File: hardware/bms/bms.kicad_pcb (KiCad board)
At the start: 2 copper layers, 199 parts, among them J1 Conn_01x08, J10 Conn_01x02, J11 Conn_01x02, J12 Conn_01x02, J13 Conn_01x10, J14 Conn_01x02, J15 Conn_01x02, J16 Cell Bypass, J2 Conn_01x04, J3 USB_B_Micro, J4 Conn_01x05, J5 Conn_01x04, J6 Conn_01x04, J7 Conn_01x03, J8 Conn_01x03, J9 Conn_01x02, M1 MountingHole, M2 MountingHole, M3 MountingHole, M4 MountingHole, M5 MountingHole, M6 MountingHole, Q1 BC817, Q10 ZXMP4A16G, Q11 IRF540N, Q12 IRF540N, Q13 BSS138, Q14 IRF540N, Q15 BSS138, Q16 BSS138, Q2 ZXMP4A16G, Q3 BSS138, Q4 BS170, Q5 IRF9540N, Q6 BC847, Q7 IRF9540N, Q8 BSS138, Q9 ZXMP4A16G, SW1 SW_DIP_x03, U1 USBLC6-2SC6, U2 STM32F042C6Tx, U3 TPS560430x3F, U4 TCAN334, U5 MAX485E, U6 LM5164DDAR, U7 LSI94202, Y1 8MHz

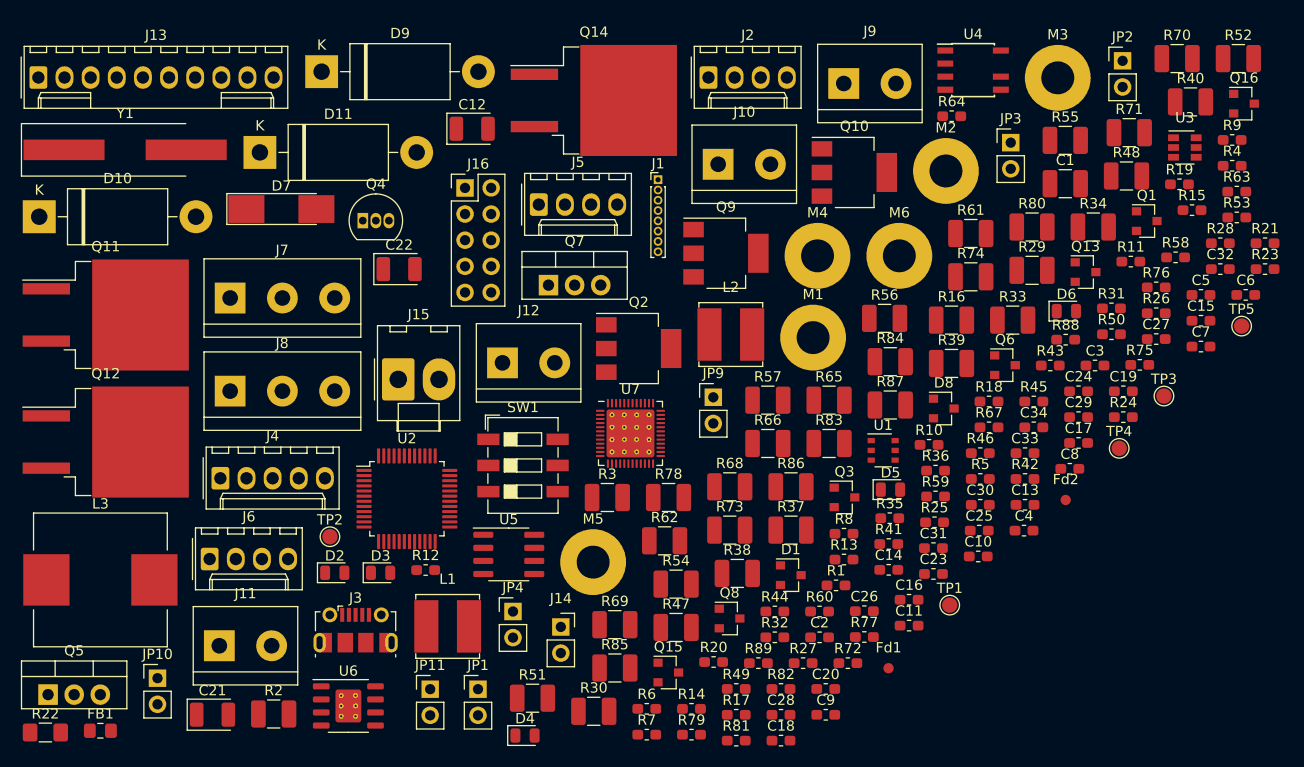
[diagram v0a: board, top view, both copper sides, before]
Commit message: footprint corrections
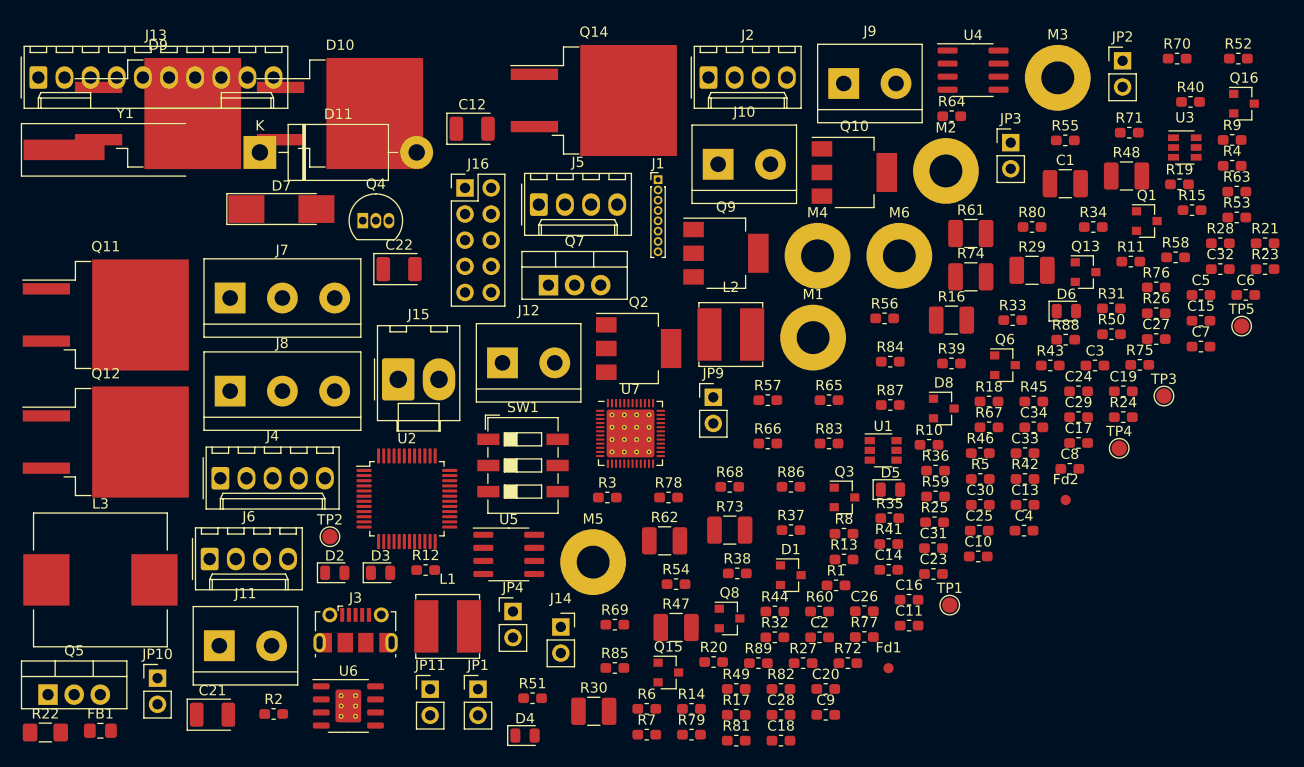
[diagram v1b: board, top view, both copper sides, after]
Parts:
- D10, D9: value MBR340 -> 200V_Diode; footprint Diode_THT:D_DO-201AD_P15.24mm_Horizontal -> bms:D2PAK
- R2, R3, R33, R34, R37, R38, R39, R40, R51, R52, R54, R55, R56, R57, R65, R66, R68, R69, R70, R71, R78, R80, R83, R84, R85, R86, R87: footprint Resistor_SMD:R_1210_3225Metric_Pad1.42x2.65mm_HandSolder -> Resistor_SMD:R_0603_1608Metric_Pad1.05x0.95mm_HandSolder
- R35: value 1K -> 10K
- U1: footprint Package_SO:TSOP-6_1.65x3.05mm_P0.95mm -> Package_TO_SOT_SMD:SuperSOT-6
- U4: footprint Package_SO:SOIC-8-N7_3.9x4.9mm_P1.27mm -> Package_SO:SOIC-8_3.9x4.9mm_P1.27mm
- moved D10 30.9 mm to (177.2, 75.5)
- moved D9 16.4 mm to (159.5, 75.5)
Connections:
- C23 pad 1: PWR- -> Net-(C23-Pad1)
- D10 pad 1: Net-(D10-Pad1) -> PWR-
- D9 pad 1: Net-(C16-Pad2) -> Net-(D9-Pad1)
- L3 pad 1: Net-(D10-Pad1) -> Net-(D10-Pad4)
- Q1 pad 2: Net-(D9-Pad2) -> Net-(D9-Pad1)
- Q14 pad 2: LOAD -> CS2
- Q14 pad 3: CS1 -> LOAD
- Q5 pad 1: Net-(D9-Pad2) -> Net-(D9-Pad1)
- Q5 pad 2: Net-(D10-Pad1) -> Net-(D10-Pad4)
- Q7 pad 1: PWR- -> Net-(C23-Pad1)
- R35 pad 2: Net-(D9-Pad2) -> Net-(D9-Pad1)
- R36 pad 1: Net-(D9-Pad2) -> Net-(D9-Pad1)
- R46 pad 1: PWR- -> Net-(C23-Pad1)
- R89 pad 2: LOAD -> CHG

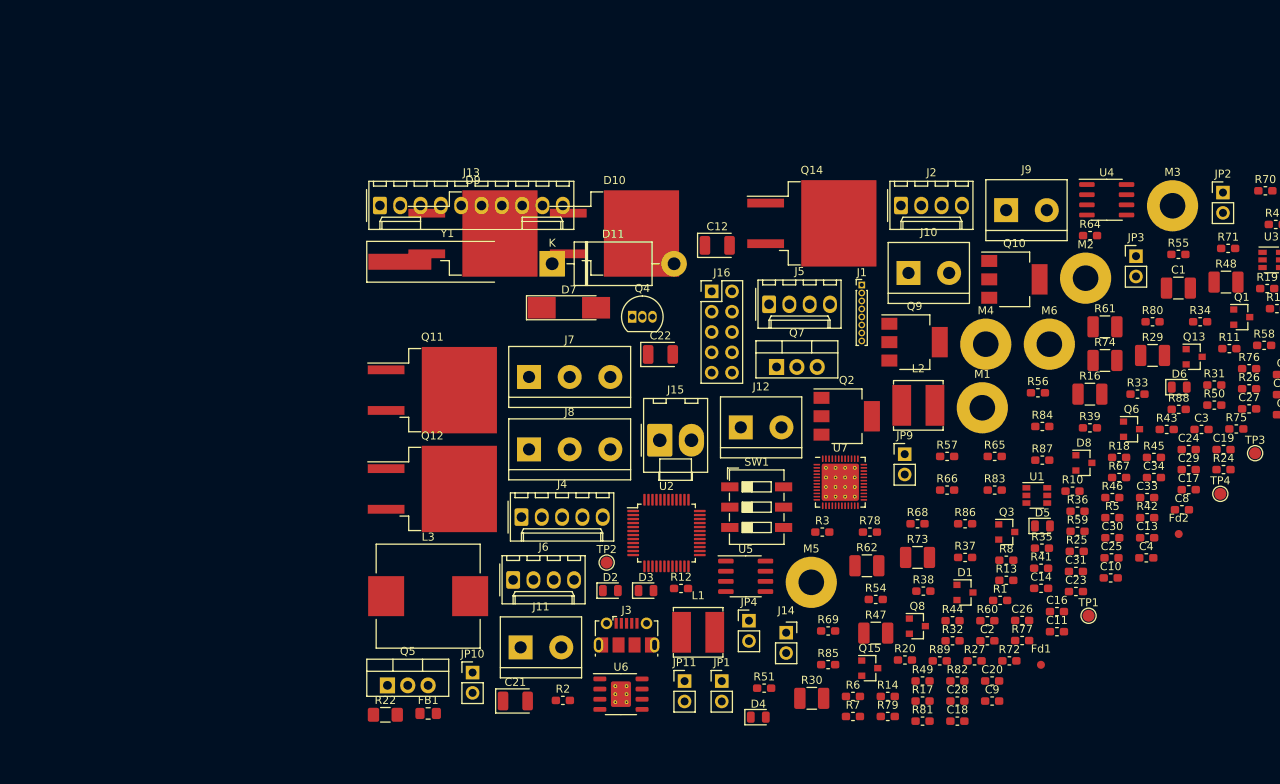
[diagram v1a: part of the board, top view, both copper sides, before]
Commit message: Added i2c level shifter
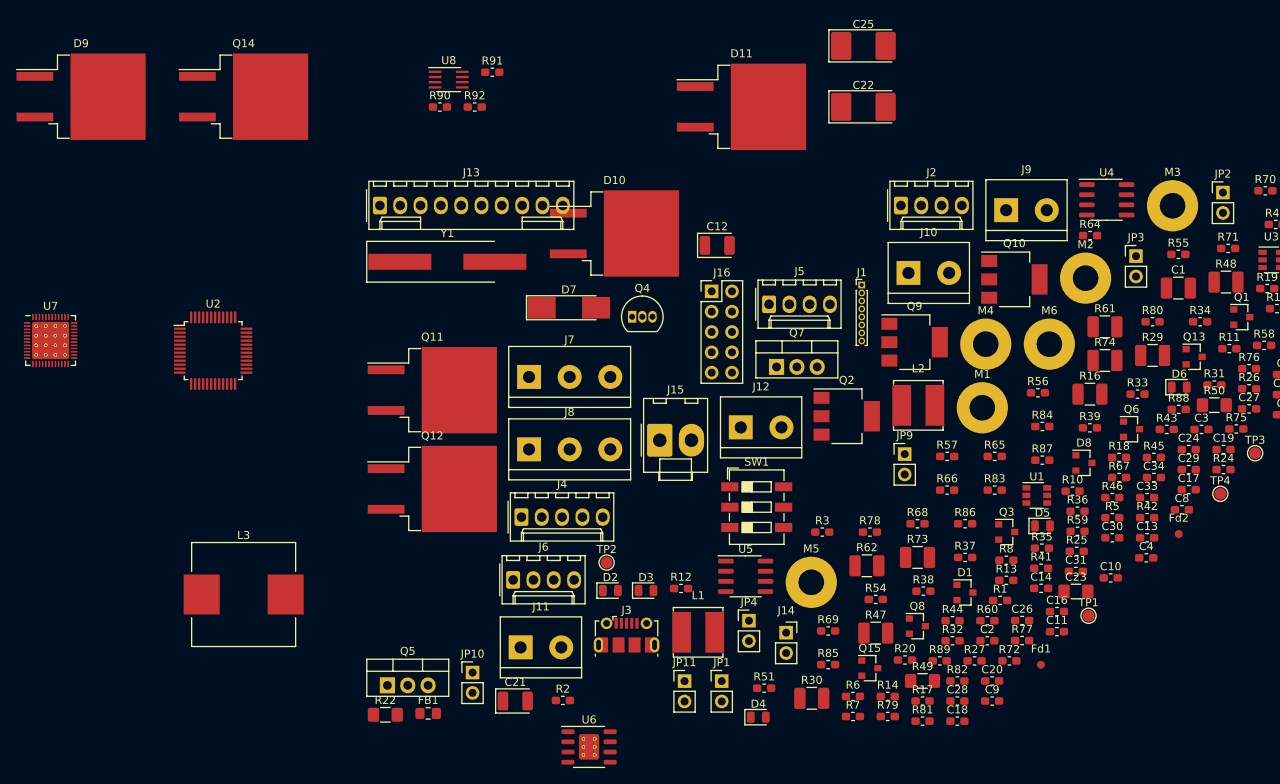
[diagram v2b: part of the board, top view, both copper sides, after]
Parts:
- added R90: 4K7, Resistor_SMD:R_0603_1608Metric_Pad1.05x0.95mm_HandSolder, F.Cu at (155.3, 59.7)
- added R91: 4K7, Resistor_SMD:R_0603_1608Metric_Pad1.05x0.95mm_HandSolder, F.Cu at (161.9, 55.4)
- added R92: 200K, Resistor_SMD:R_0603_1608Metric_Pad1.05x0.95mm_HandSolder, F.Cu at (159.7, 59.7)
- added U8: PCA9306, Package_SO:SSOP-8_2.95x2.8mm_P0.65mm, F.Cu at (156.4, 56.3)
- C22: value 330uF -> 10uF; footprint Capacitor_Tantalum_SMD:CP_EIA-3528-21_Kemet-B -> Capacitor_Tantalum_SMD:CP_EIA-7132-28_AVX-C
- C23: value 10nF -> 0.01uF; footprint Capacitor_SMD:C_0603_1608Metric_Pad1.05x0.95mm_HandSolder -> Capacitor_SMD:C_1206_3216Metric_Pad1.42x1.75mm_HandSolder
- C25: value 2.2uF -> 10uF; footprint Capacitor_SMD:C_0603_1608Metric_Pad1.05x0.95mm_HandSolder -> Capacitor_Tantalum_SMD:CP_EIA-7132-28_AVX-C
- D11: value MBR340 -> 200V_Diode; footprint Diode_THT:D_DO-201AD_P15.24mm_Horizontal -> bms:D2PAK
- R49, R50: footprint Resistor_SMD:R_0603_1608Metric_Pad1.05x0.95mm_HandSolder -> Resistor_SMD:R_1206_3216Metric_Pad1.42x1.75mm_HandSolder
- R6, R9: value 2K2 -> 4K7
- moved U7 100.3 mm to (106.7, 88.9)
- moved Q14 72.8 mm to (130.8, 58.4)
- moved C25 71.1 mm to (208.3, 52.1)
- moved U2 61.1 mm to (127.0, 90.2)
- moved D9 51.9 mm to (110.5, 58.4)
- moved C22 40.0 mm to (208.3, 59.7)
- moved D11 30.7 mm to (193.0, 59.7)
- moved L3 23.1 mm to (130.8, 120.7)
- moved U6 7.71 mm to (174.0, 139.7)
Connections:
- net Net-(TP5-Pad1) renamed RGO
- C25 pad 1: PWR- -> Net-(C22-Pad1)
- C25 pad 2: Net-(C22-Pad1) -> PWR-
- D11 pad 1: PWR_OUT -> Net-(C22-Pad1)
- R6 pad 1: SDA -> SDA_3.3
- R89 pad 2: CHG -> LOAD
- R9 pad 1: SCL -> SCL_3.3
- U2 pad 42: SCL -> SCL_3.3
- U2 pad 43: SDA -> SDA_3.3
- U7 pad 49: (no net) -> GND

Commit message: Schematics and footprint corrections
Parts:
- added FB2: Ferrite_Bead_Small, Inductor_SMD:L_0805_2012Metric_Pad1.15x1.40mm_HandSolder, F.Cu at (96.5, 156.2)
- added NT1: Net-Tie_2, NetTie:NetTie-2_THT_Pad1.0mm, F.Cu at (248.9, 128.3)
- Q10, Q2, Q9: value ZXMP4A16G -> NX3008PBK; footprint Package_TO_SOT_SMD:SOT-223-3_TabPin2 -> Package_TO_SOT_SMD:SOT-23
- Q4: footprint Package_TO_SOT_THT:TO-92_Inline -> Package_TO_SOT_SMD:SOT-23W_Handsoldering
- Q5, Q7: footprint Package_TO_SOT_THT:TO-220-3_Vertical -> Package_TO_SOT_SMD:TO-263-2
- moved U3 217.9 mm to (54.6, 153.7)
- moved C1 216.7 mm to (44.5, 157.5)
- moved C3 207.7 mm to (49.5, 152.4)
- moved R4 202.2 mm to (82.5, 170.2)
- moved R43 199.4 mm to (47.0, 90.2)
- moved C8 199.2 mm to (54.6, 157.5)
- moved R46 198.0 mm to (41.9, 94.0)
- moved C23 195.3 mm to (41.9, 90.2)
- moved R9 194.9 mm to (84.2, 153.7)
- moved R16 190.3 mm to (58.4, 162.6)
- moved R53 189.7 mm to (77.5, 118.1)
- moved Q6 188.6 mm to (53.3, 91.4)
- moved R41 185.0 mm to (47.0, 94.0)
- moved R23 184.6 mm to (83.8, 68.6)
- moved C15 183.4 mm to (81.3, 58.4)
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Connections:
- C10 pad 2: GND -> GNDS
- C18 pad 2: GND -> GNDA
- C19 pad 2: GND -> GNDA
- C26 pad 2: GND -> GNDA
- C27 pad 2: GND -> GNDA
- C31 pad 2: GND -> GNDA
- C32 pad 2: GND -> GNDA
- C33 pad 2: GND -> GNDA
- C34 pad 2: GND -> GNDA
- JP10 pad 2: GND -> GNDA
- JP3 pad 2: GND -> GNDA
- R50 pad 1: GND -> GNDA
- R76 pad 1: VCC -> RGO
- R77 pad 1: VCC -> RGO
- R79 pad 1: VCC -> RGO
- R82 pad 1: VCC -> RGO
- R88 pad 2: GND -> GNDA
- U2 pad 8: GNDA -> GNDS
- U7 pad 18: GND -> GNDA
- U7 pad 28: GND -> GNDA
- U7 pad 29: GND -> GNDA
- U7 pad 49: GND -> GNDA

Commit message: Started placement
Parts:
- C16, C22, C25, C34, D10, L3, Q4, R29, R30, R33, R34, R37, R39, R47, R48, R51, R52, R54, R56, R61, R62, R65, R66, R68, R70, R73, R74, R78, R83, R87: moved to B.Cu
- moved JP9 121.1 mm to (53.0, 80.7), turned to 90 degrees
- moved Q16 115.5 mm to (193.6, 148.3)
- moved C12 112.7 mm to (105.6, 62.0), turned to 0 degrees
- moved JP3 112.0 mm to (73.4, 80.5), turned to 90 degrees
- moved D10 111.1 mm to (30.3, 45.3)
- moved TP1 109.7 mm to (109.7, 63.0)
- moved R16 107.8 mm to (105.7, 65.7), turned to 180 degrees
- moved D11 107.8 mm to (30.4, 69.5)
- moved JP2 104.9 mm to (65.1, 80.3), turned to 90 degrees
- moved C22 103.4 mm to (27.0, 71.0)
- moved Q13 103.2 mm to (200.0, 141.5)
- moved Q8 102.9 mm to (207.8, 148.4)
- moved C1 102.8 mm to (101.5, 72.0), turned to 270 degrees
- moved D1 102.7 mm to (105.2, 69.5), turned to 270 degrees
- moved Q1 102.3 mm to (17.0, 48.2)
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
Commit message: Changed placement
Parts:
- moved Q12 47.3 mm to (49.0, 87.3), turned to 180 degrees
- moved R64 41.5 mm to (51.5, 60.5), turned to 0 degrees
- moved R59 40.2 mm to (51.5, 58.2), turned to 0 degrees
- moved C28 34.1 mm to (55.6, 58.2), turned to 180 degrees
- moved C14 33.1 mm to (63.1, 45.7)
- moved C15 33.1 mm to (77.4, 42.6)
- moved C20 33.1 mm to (85.0, 42.6)
- moved C21 33.1 mm to (89.0, 44.5)
- moved D7 33.1 mm to (69.7, 41.9)
- moved L2 33.1 mm to (83.1, 47.2)
- moved R22 33.1 mm to (66.4, 46.5)
- moved R23 33.1 mm to (68.8, 47.3)
- moved R31 33.1 mm to (81.3, 42.6)
- moved R44 33.1 mm to (78.9, 52.1)
- moved R45 33.1 mm to (74.8, 52.1)
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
